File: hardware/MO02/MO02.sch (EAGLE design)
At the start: 25 parts, among them J1 AUDIO-JACK2PTH, J2 M04X2, Q1 G2XX3---PW20, Q2 32.768 kHz, SW1 DTS-6

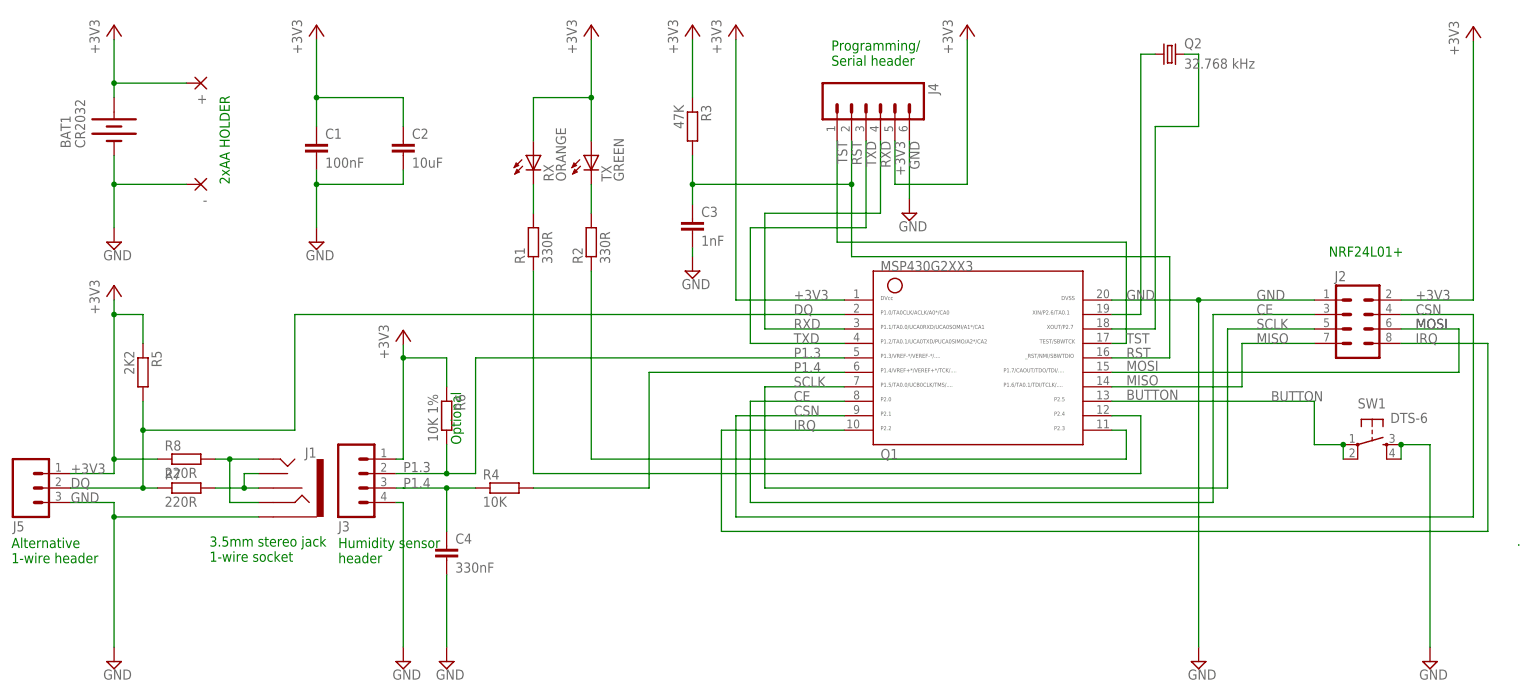
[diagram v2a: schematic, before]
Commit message: 2x3 programming/serial header, SMD switch at side of board
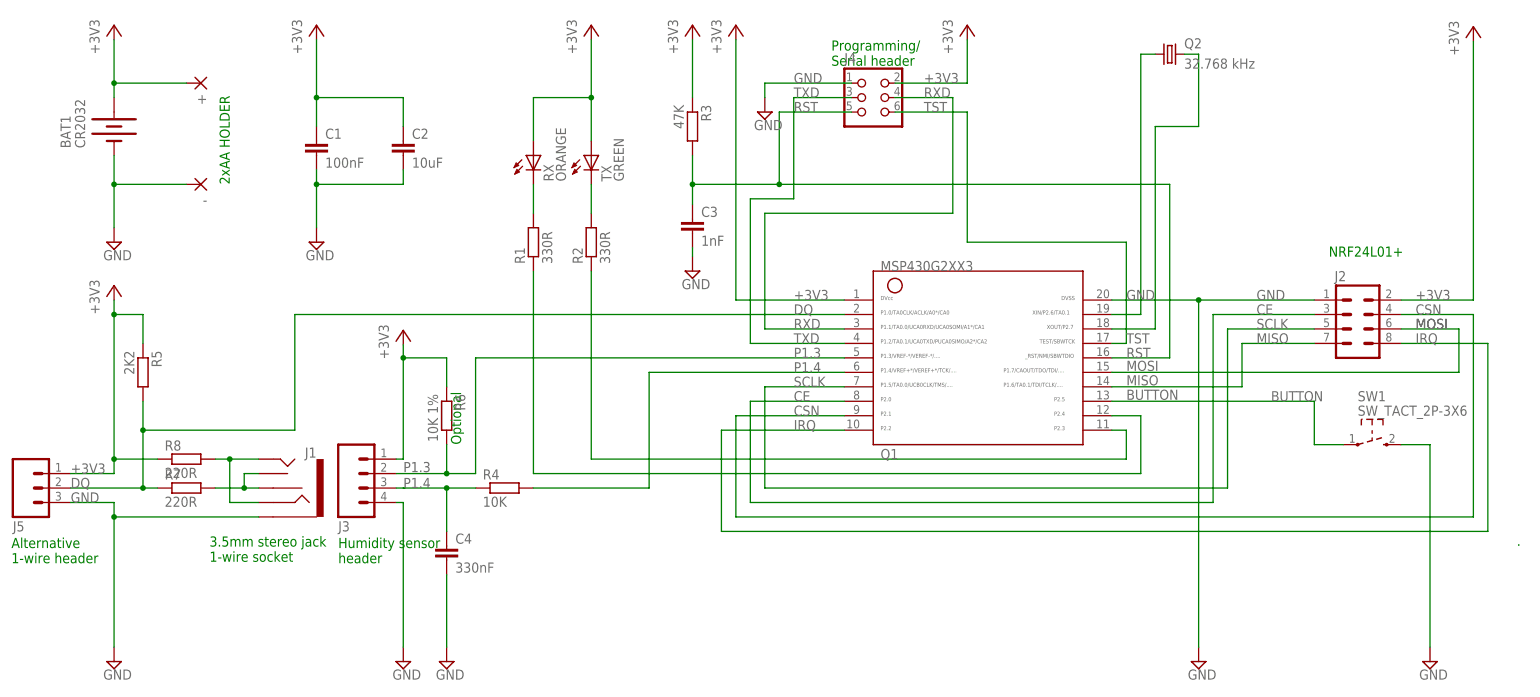
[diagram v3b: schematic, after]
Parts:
- J4: value (none) -> CON_HEADER_2X03-PTH; device SparkFun:M06SIP -> dp_devices:CON_HEADER_2X03-PTH
- SW1: value DTS-6 -> SW_TACT_2P-3X6; device switch-tact:DTS-6 -> dp_devices:SW_TACT_2P-3X6
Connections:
- net +3V3: now also J4.2; no longer J4.5
- net BUTTON: no longer SW1.2
- net GND: now also J4.1; no longer J4.6, SW1.4
- net RST: now also J4.5; no longer J4.2
- net TST: now also J4.6; no longer J4.1
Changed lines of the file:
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@@
 <attribute name="RESISTANCE" value="4K7"/>
 </part>
-<part name="J4" library="SparkFun" deviceset="M06" device="SIP"/>
 <part name="P+11" library="supply1" deviceset="+3V3" device=""/>
 <part name="R6" library="resistor" deviceset="R-EU_" device="M0805" value="10K 1%">
@@
 <part name="J5" library="SparkFun" deviceset="M03" device="PTH"/>
 <part name="P+4" library="supply1" deviceset="+3V3" device=""/>
-<part name="SW1" library="switch-tact" deviceset="DTS-6" device=""/>
 <part name="GND3" library="supply2" deviceset="GND" device=""/>
 <part name="-" library="wirepad" deviceset="2,54/1,0" device=""/>
@@
 <attribute name="RESISTANCE" value="4K7"/>
 </part>
+<part name="SW1" library="dp_devices" deviceset="SW_TACT_2P" device="-3X6"/>
+<part name="J4" library="dp_devices" deviceset="CON_HEADER_2X03" device="-PTH"/>
 </parts>
 <sheets>
@@
 <instance part="P+10" gate="G$1" x="134.62" y="139.7"/>
 <instance part="R3" gate="G$1" x="134.62" y="121.92" rot="R270"/>
-<instance part="J4" gate="G$1" x="165.1" y="124.46" rot="R270"/>
 <instance part="P+11" gate="G$1" x="182.88" y="139.7"/>
 <instance part="R6" gate="G$1" x="91.44" y="71.12" rot="R270"/>
-<instance part="GND12" gate="GND" x="172.72" y="106.68"/>
+<instance part="GND12" gate="GND" x="147.32" y="124.46"/>
 <instance part="J5" gate="G$1" x="17.78" y="58.42" rot="MR180"/>
 <instance part="P+4" gate="G$1" x="116.84" y="139.7"/>
-<instance part="SW1" gate="G$1" x="254" y="66.04" rot="R270"/>
 <instance part="GND3" gate="GND" x="33.02" y="101.6"/>
 <instance part="-" gate="P" x="48.26" y="111.76" rot="R180"/>
@@
 <instance part="R8" gate="G$1" x="45.72" y="63.5"/>
 <instance part="R7" gate="G$1" x="45.72" y="58.42"/>
+<instance part="SW1" gate="SW" x="254" y="66.04"/>
+<instance part="J4" gate="J" x="162.56" y="127"/>
 </instances>
 <busses>
@@
 </segment>
 <segment>
-<pinref part="J4" gate="G$1" pin="5"/>
-<wire x1="170.18" y1="119.38" x2="170.18" y2="111.76" width="0.1524" layer="91"/>
 <pinref part="P+11" gate="G$1" pin="+3V3"/>
-<wire x1="170.18" y1="111.76" x2="182.88" y2="111.76" width="0.1524" layer="91"/>
-<wire x1="182.88" y1="111.76" x2="182.88" y2="137.16" width="0.1524" layer="91"/>
-<label x="170.18" y="119.38" size="1.778" layer="95" rot="R270"/>
+<wire x1="182.88" y1="129.54" x2="182.88" y2="137.16" width="0.1524" layer="91"/>
+<wire x1="182.88" y1="129.54" x2="170.18" y2="129.54" width="0.1524" layer="91"/>
+<label x="175.26" y="129.54" size="1.778" layer="95"/>
+<pinref part="J4" gate="J" pin="2"/>
 </segment>
 <segment>
@@
 <pinref part="Q1" gate="G$1" pin="16"/>
 <wire x1="208.28" y1="81.28" x2="218.44" y2="81.28" width="0.1524" layer="91"/>
-<pinref part="J4" gate="G$1" pin="2"/>
-<wire x1="218.44" y1="99.06" x2="218.44" y2="81.28" width="0.1524" layer="91"/>
-<wire x1="162.56" y1="119.38" x2="162.56" y2="111.76" width="0.1524" layer="91"/>
-<wire x1="162.56" y1="111.76" x2="162.56" y2="99.06" width="0.1524" layer="91"/>
-<wire x1="162.56" y1="99.06" x2="218.44" y2="99.06" width="0.1524" layer="91"/>
-<label x="162.56" y="119.38" size="1.778" layer="95" rot="R270"/>
+<wire x1="218.44" y1="111.76" x2="218.44" y2="81.28" width="0.1524" layer="91"/>
 <label x="210.82" y="81.28" size="1.778" layer="95"/>
 <pinref part="R3" gate="G$1" pin="2"/>
-<wire x1="162.56" y1="111.76" x2="134.62" y2="111.76" width="0.1524" layer="91"/>
+<wire x1="149.86" y1="111.76" x2="134.62" y2="111.76" width="0.1524" layer="91"/>
 <wire x1="134.62" y1="111.76" x2="134.62" y2="116.84" width="0.1524" layer="91"/>
 <wire x1="134.62" y1="108.204" x2="134.62" y2="111.76" width="0.1524" layer="91"/>
 <pinref part="C3" gate="G$1" pin="1"/>
 <junction x="134.62" y="111.76"/>
-<junction x="162.56" y="111.76"/>
+<wire x1="149.86" y1="111.76" x2="218.44" y2="111.76" width="0.1524" layer="91"/>
+<wire x1="162.56" y1="124.46" x2="149.86" y2="124.46" width="0.1524" layer="91"/>
+<wire x1="149.86" y1="124.46" x2="149.86" y2="111.76" width="0.1524" layer="91"/>
+<label x="152.4" y="124.46" size="1.778" layer="95"/>
+<junction x="149.86" y="111.76"/>
+<pinref part="J4" gate="J" pin="5"/>
 </segment>
 </net>
@@
 <wire x1="208.28" y1="83.82" x2="210.82" y2="83.82" width="0.1524" layer="91"/>
 <wire x1="210.82" y1="83.82" x2="210.82" y2="101.6" width="0.1524" layer="91"/>
-<pinref part="J4" gate="G$1" pin="1"/>
-<wire x1="210.82" y1="101.6" x2="160.02" y2="101.6" width="0.1524" layer="91"/>
-<wire x1="160.02" y1="101.6" x2="160.02" y2="119.38" width="0.1524" layer="91"/>
+<wire x1="210.82" y1="101.6" x2="182.88" y2="101.6" width="0.1524" layer="91"/>
 <label x="210.82" y="83.82" size="1.778" layer="95"/>
-<label x="160.02" y="119.38" size="1.778" layer="95" rot="R270"/>
+<wire x1="170.18" y1="124.46" x2="182.88" y2="124.46" width="0.1524" layer="91"/>
+<wire x1="182.88" y1="124.46" x2="182.88" y2="101.6" width="0.1524" layer="91"/>
+<label x="175.26" y="124.46" size="1.778" layer="95"/>
+<pinref part="J4" gate="J" pin="6"/>
 </segment>
 </net>
@@
 <segment>
 <wire x1="161.29" y1="83.82" x2="144.78" y2="83.82" width="0.1524" layer="91"/>
-<wire x1="144.78" y1="83.82" x2="144.78" y2="104.14" width="0.1524" layer="91"/>
-<pinref part="J4" gate="G$1" pin="3"/>
-<wire x1="144.78" y1="104.14" x2="165.1" y2="104.14" width="0.1524" layer="91"/>
-<wire x1="165.1" y1="104.14" x2="165.1" y2="119.38" width="0.1524" layer="91"/>
+<wire x1="144.78" y1="83.82" x2="144.78" y2="109.22" width="0.1524" layer="91"/>
+<wire x1="144.78" y1="109.22" x2="152.4" y2="109.22" width="0.1524" layer="91"/>
 <pinref part="Q1" gate="G$1" pin="4"/>
 <label x="152.4" y="83.82" size="1.778" layer="95"/>
-<label x="165.1" y="119.38" size="1.778" layer="95" rot="R270"/>
+<wire x1="152.4" y1="109.22" x2="152.4" y2="127" width="0.1524" layer="91"/>
+<label x="152.4" y="127" size="1.778" layer="95"/>
+<wire x1="152.4" y1="127" x2="162.56" y2="127" width="0.1524" layer="91"/>
+<pinref part="J4" gate="J" pin="3"/>
 </segment>
 </net>
@@
 <wire x1="161.29" y1="86.36" x2="147.32" y2="86.36" width="0.1524" layer="91"/>
 <wire x1="147.32" y1="86.36" x2="147.32" y2="106.68" width="0.1524" layer="91"/>
-<pinref part="J4" gate="G$1" pin="4"/>
-<wire x1="147.32" y1="106.68" x2="167.64" y2="106.68" width="0.1524" layer="91"/>
-<wire x1="167.64" y1="106.68" x2="167.64" y2="119.38" width="0.1524" layer="91"/>
+<wire x1="147.32" y1="106.68" x2="180.34" y2="106.68" width="0.1524" layer="91"/>
 <pinref part="Q1" gate="G$1" pin="3"/>
 <label x="152.4" y="86.36" size="1.778" layer="95"/>
-<label x="167.64" y="119.38" size="1.778" layer="95" rot="R270"/>
+<wire x1="180.34" y1="127" x2="180.34" y2="106.68" width="0.1524" layer="91"/>
+<label x="175.26" y="127" size="1.778" layer="95"/>
+<wire x1="170.18" y1="127" x2="180.34" y2="127" width="0.1524" layer="91"/>
+<pinref part="J4" gate="J" pin="4"/>
 </segment>
 </net>
@@
 <label x="210.82" y="73.914" size="1.778" layer="95"/>
 <label x="236.22" y="73.66" size="1.778" layer="95"/>
-<pinref part="SW1" gate="G$1" pin="2"/>
-<pinref part="SW1" gate="G$1" pin="1"/>
-<wire x1="248.92" y1="66.04" x2="248.92" y2="63.5" width="0.1524" layer="91"/>
 <wire x1="248.92" y1="66.04" x2="243.84" y2="66.04" width="0.1524" layer="91"/>
 <wire x1="243.84" y1="66.04" x2="243.84" y2="73.66" width="0.1524" layer="91"/>
-<junction x="248.92" y="66.04"/>
+<pinref part="SW1" gate="SW" pin="1"/>
 </segment>
 </net>
@@
 <segment>
 <pinref part="GND12" gate="GND" pin="GND"/>
-<pinref part="J4" gate="G$1" pin="6"/>
-<wire x1="172.72" y1="109.22" x2="172.72" y2="119.38" width="0.1524" layer="91"/>
-<label x="172.72" y="119.38" size="1.778" layer="95" rot="R270"/>
+<wire x1="147.32" y1="127" x2="147.32" y2="129.54" width="0.1524" layer="91"/>
+<label x="152.4" y="129.54" size="1.778" layer="95"/>
+<wire x1="162.56" y1="129.54" x2="147.32" y2="129.54" width="0.1524" layer="91"/>
+<pinref part="J4" gate="J" pin="1"/>
 </segment>
 <segment>
@@
 </segment>
 <segment>
-<pinref part="SW1" gate="G$1" pin="3"/>
-<pinref part="SW1" gate="G$1" pin="4"/>
-<wire x1="259.08" y1="63.5" x2="259.08" y2="66.04" width="0.1524" layer="91"/>
 <wire x1="259.08" y1="66.04" x2="264.16" y2="66.04" width="0.1524" layer="91"/>
 <pinref part="GND2" gate="GND" pin="GND"/>
 <wire x1="264.16" y1="30.48" x2="264.16" y2="66.04" width="0.1524" layer="91"/>
-<junction x="259.08" y="66.04"/>
-</segment>
-</net>
+<pinref part="SW1" gate="SW" pin="3"/>
+</segment>
+</net>
